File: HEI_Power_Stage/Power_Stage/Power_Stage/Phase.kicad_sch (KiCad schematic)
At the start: 34 parts, among them Q1 EPC2304ENGRT, Q2 EPC2304ENGRT, T1 30k, T2 30k, U2 NCP51820AMNTWG, U6 ADC124S051CIMM/NOPB

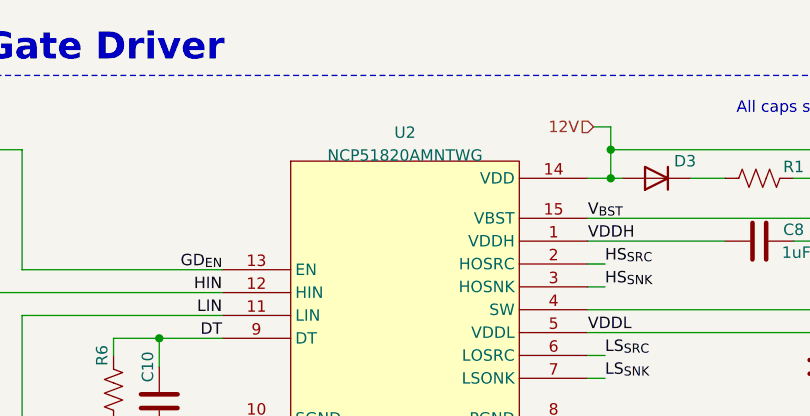
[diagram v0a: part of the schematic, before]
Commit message: initial phase a routing
routed connections for phase A not including SPI. spi left as stubs that can be routed to connector and to the other ADCs.
Power and PWRGND routing is done on layer 1,2,4 and can be discussed further in persons. For now I have VDC on layer 1 and 4. PWRGND on layer 1 and 4. SW and PHA on layer 1 and 2. layer 3 and 5 are gnd. Layer 1 and 6 are signal.
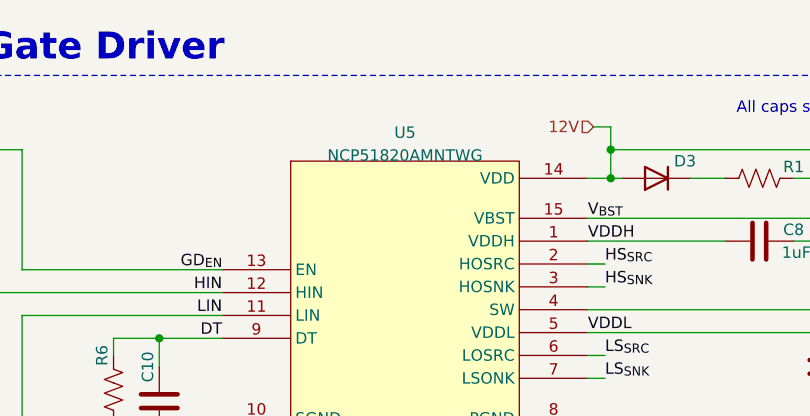
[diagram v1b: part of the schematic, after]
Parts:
- renumbered TP1 to TP5, TP2 to TP6, U2 to U5

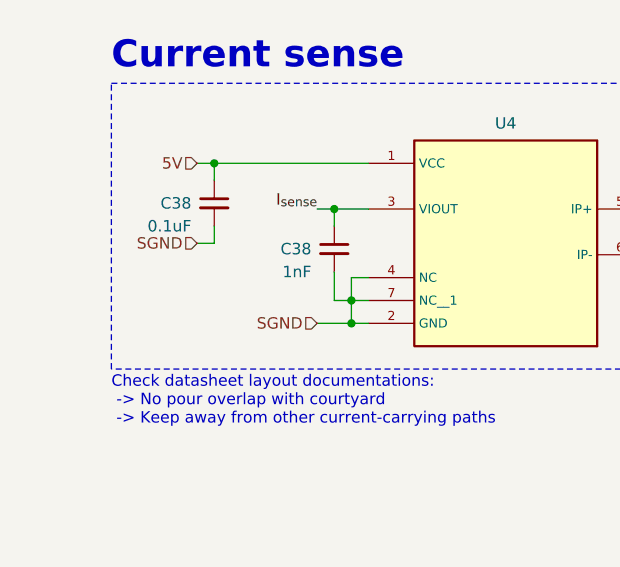
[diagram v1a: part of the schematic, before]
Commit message: layout
5v regulators for each phase daq
12v iso
top half and bottom half planes
SPi goes from bottom to top layer at plane split
power routed on bottom two layers with solid planes
switch nodes on top two layers
4 adcs now
daq for dc input
current sensors now references to gndpwr
Still need to figure out how to connect gndpwr pours with isolation
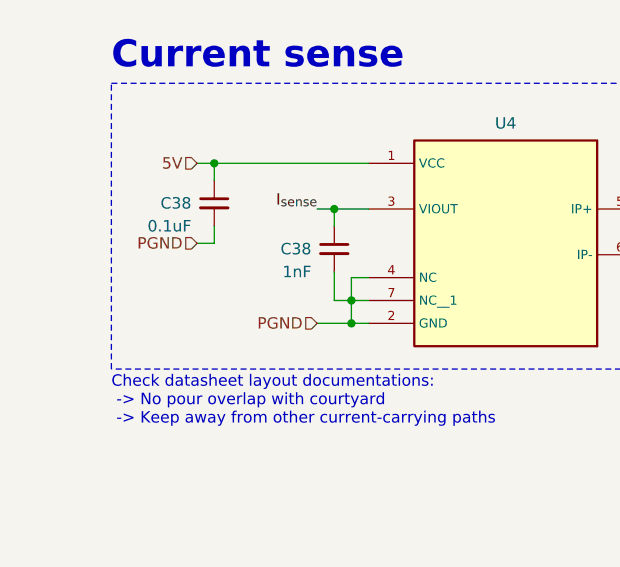
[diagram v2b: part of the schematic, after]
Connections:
- net PGND: now also C38.2, C38.2, U4.2 (GND), U4.4 (NC), U4.7 (NC__1)
- net SGND: no longer C38.2, C38.2, U4.2 (GND), U4.4 (NC), U4.7 (NC__1)
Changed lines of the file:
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@@
 		)
 	)
-	(hierarchical_label "SGND"
+	(hierarchical_label "PGND"
 		(shape input)
 		(at 39.37 137.795 180)
@@
 		)
 	)
-	(hierarchical_label "SGND"
+	(hierarchical_label "PGND"
 		(shape input)
 		(at 52.705 146.685 180)

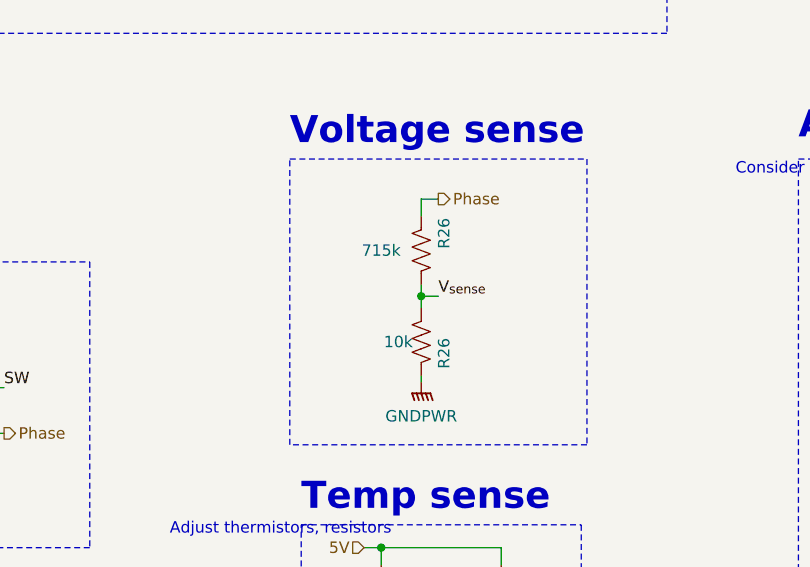
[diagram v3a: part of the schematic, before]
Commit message: POC layout changes fro meeting
Two cap options on the bottom:
large kemet that would meet all requirements on its own
also large cylindrical aluminum electrolytic that only has 4.3A riplpe current rating. can use either for testing. can also add more holes for trying other caps

layer 3 now continous gndpwr for whole board.
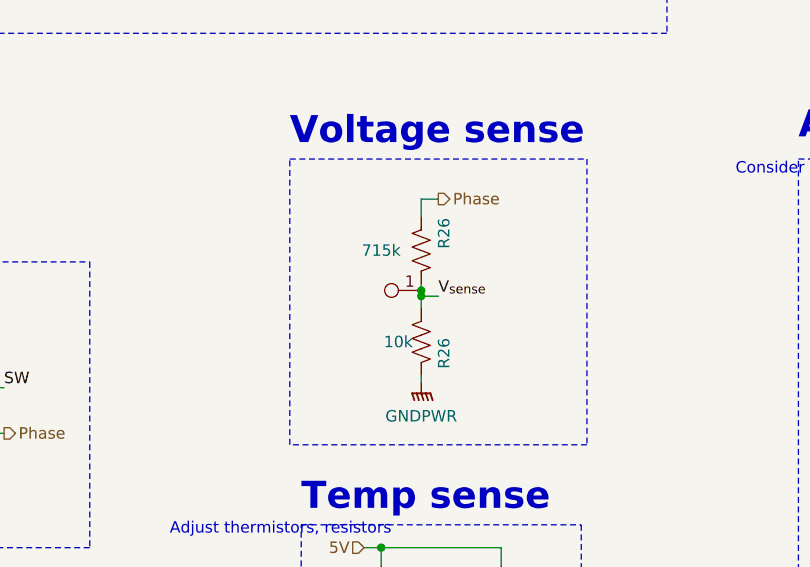
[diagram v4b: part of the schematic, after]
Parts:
- added TP11: Test_Point, TestPoint:TestPoint_Pad_D1.0mm, symbol GTSR_symbol_lib:Test_Point
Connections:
- net V_{sense}: now also TP11.1
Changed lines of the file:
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@@
 	)
 	(junction
+		(at 137.16 123.19)
+		(diameter 0)
+		(color 0 0 0 0)
+	)
+	(junction
 		(at 46.355 63.5)
 		(diameter 0)
@@
 	(wire
 		(pts
-			(xy 137.16 122.555) (xy 137.16 123.825)
+			(xy 137.16 122.555) (xy 137.16 123.19)
 		)
 		(stroke
@@
 	(wire
 		(pts
+			(xy 137.16 123.19) (xy 137.16 123.825)
+		)
+		(stroke
+			(width 0)
+			(type default)
+		)
+	)
+	(wire
+		(pts
 			(xy 132.715 151.765) (xy 132.715 153.67)
 		)
@@
 					(unit 1)
 				)
+			)
+		)
+	)
+	(symbol
+		(lib_id "GTSR_symbol_lib:Test_Point")
+		(at 137.16 123.19 90)
+		(unit 1)
+		(exclude_from_sim no)
+		(in_bom yes)
+		(on_board yes)
+		(dnp no)
+		(property "Reference" "TP11"
+			(at 133.985 121.92 0)
+			(effects
+				(font
+					(size 1.27 1.27)
+				)
+				(justify left)
+				(hide yes)
+			)
+		)
+		(property "Value" "Test_Point"
+			(at 135.1279 120.65 0)
+			(effects
+				(font
+					(size 1.27 1.27)
+				)
+				(justify left)
+				(hide yes)
+			)
+		)
+		(property "Footprint" "TestPoint:TestPoint_Pad_D1.0mm"
+			(at 144.78 123.19 0)
+			(effects
+				(font
+					(size 1.27 1.27)
+				)
+				(hide yes)
+			)
+		)
+		(property "Datasheet" ""
+			(at 144.78 123.19 0)
+			(effects
+				(font
+					(size 1.27 1.27)
+				)
+				(hide yes)
+			)
+		)
+		(property "Description" ""
+			(at 137.16 123.19 0)
+			(effects
+				(font
+					(size 1.27 1.27)
+				)
+				(hide yes)
+			)
+		)
+		(pin "1"
+		)
+		(instances
+			(project "Power_Stage"
+				(path "/4073579f-dff4-4919-be9b-9c43467e22c1/fdb1cb22-51b8-420c-a9c7-ed601f391b52"
+					(reference "TP11")
+					(unit 1)
+				)
+				(path "/4073579f-dff4-4919-be9b-9c43467e22c1/d06aea5d-6634-499e-bc84-2b0ee963ac5c"
+					(reference "TP12")
+					(unit 1)
+				)
+				(path "/4073579f-dff4-4919-be9b-9c43467e22c1/fc0c4d71-751a-405d-a2b0-dee4001cda35"
+					(reference "TP13")
+					(unit 1)
+				)

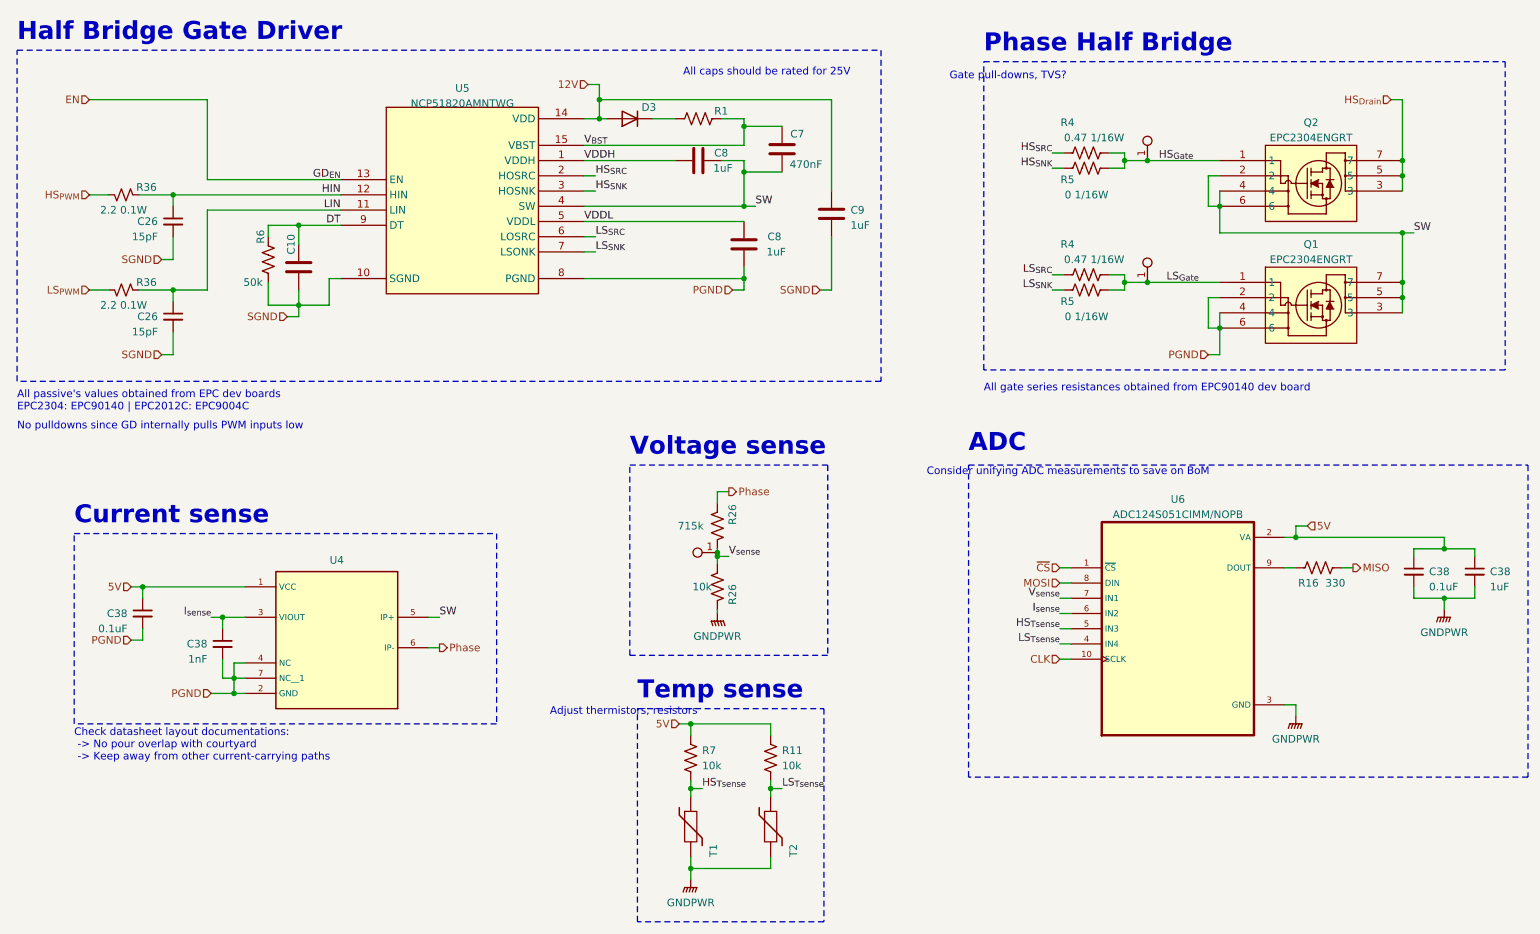
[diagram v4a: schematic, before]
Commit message: added low pass filters, PGND/SGND jumper
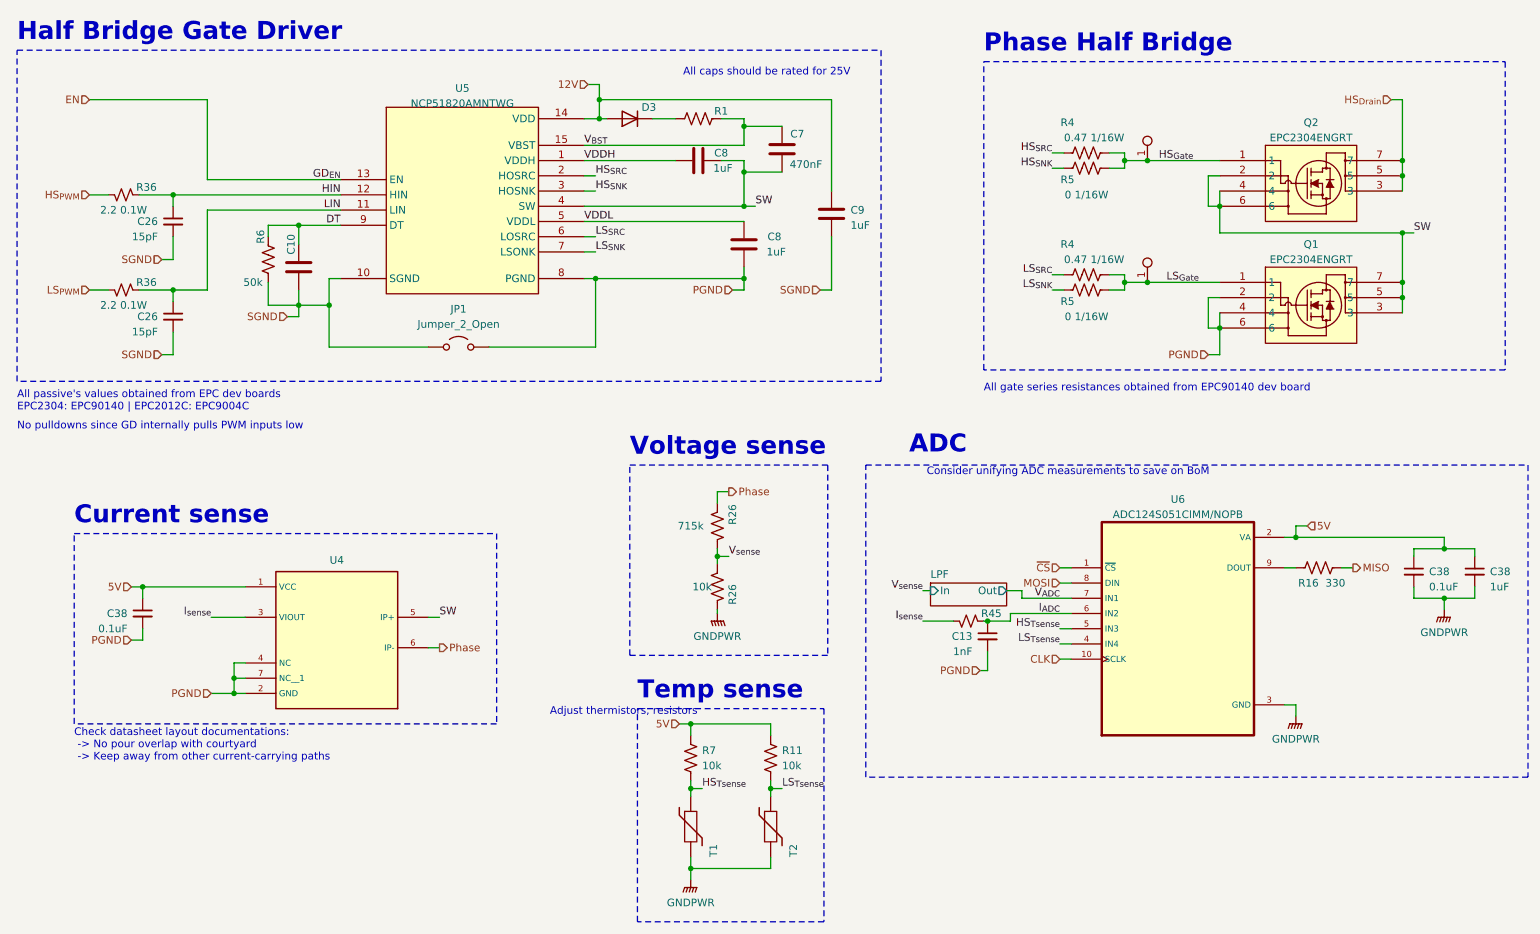
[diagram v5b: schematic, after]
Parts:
- removed C38: 1nF, Capacitor_SMD:C_0603_1608Metric_Pad1.08x0.95mm_HandSolder, symbol Device:C_Small
- removed TP11: Test_Point, TestPoint:TestPoint_Pad_D1.0mm, symbol GTSR_symbol_lib:Test_Point
- added C13: 1nF, Capacitor_SMD:C_0603_1608Metric_Pad1.08x0.95mm_HandSolder, symbol Device:C_Small
- added JP1: Jumper_2_Open, Jumper:SolderJumper-2_P1.3mm_Open_RoundedPad1.0x1.5mm, symbol Jumper:Jumper_2_Open
- added R45: 2.2 0.1W, Resistor_SMD:R_0402_1005Metric_Pad0.72x0.64mm_HandSolder, symbol Device:R_Small_US
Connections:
- net I_{sense}: now also R45.2; no longer U6.6 (IN2)
- net PGND: now also C13.2, JP1.2 (B)
- net SGND: now also JP1.1 (A)
- net V_{sense}: no longer U6.7 (IN1)
- new net I_{ADC}: C13.1, R45.1, U6.6 (IN2)
- new net V_{ADC}: U6.7 (IN1)
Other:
- added sheet LPF (LPF.kicad_sch)
- note removed: "Gate pull-downs, TVS?"

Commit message: spi isolation
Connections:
- net GNDPWR renamed HV-
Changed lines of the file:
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@@
 			)
 		)
-		(property "Value" "GNDPWR"
+		(property "Value" "HV-"
 			(at 137.16 137.16 0)
 			(effects
@@
 			)
 		)
-		(property "Value" "GNDPWR"
+		(property "Value" "HV-"
 			(at 233.68 154.305 0)
 			(effects
@@
 			)
 		)
-		(property "Value" "GNDPWR"
+		(property "Value" "HV-"
 			(at 132.715 181.61 0)
 			(effects
@@
 			)
 		)
-		(property "Value" "GNDPWR"
+		(property "Value" "HV-"
 			(at 258.445 136.525 0)
 			(effects
